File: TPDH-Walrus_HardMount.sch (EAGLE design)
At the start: 37 parts, among them Q2 DMG3404, U1 MS5803-14BA, U2 SN65HVD33RHL, U4 MCP3421A3, U5 TPS79733, U6 MAX6070AAUT18, U7 TXS0102DQM

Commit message: Initial layout for Hard mount (v0.1) variant, cleanup required
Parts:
- removed C11: 10uF, bschulz:C-EU10UFC0805
- removed C7, C8: 0.1uF, bschulz_passives:C-EU0.1UFC0402
- removed H2, H3: (no value), bschulz:MOUNTING_HOLE2_NP
- removed JP1: JUMPER-SMT_3_1-NC_PASTE_SILK, SparkFun-Jumpers:JUMPER-SMT_3_1-NC_PASTE_SILK
- removed R7: (no value), bschulz_passives:R-EU_100R0402
- removed RREF: 10k, bschulz_passives:R-EU_P10KR0603
- removed THERM: 10k, bschulz:THERMISTOR10K
- removed U6: MAX6070AAUT18, bschulz:MAX6070AAUT18
- added D2: (no value), bschulz:TVSSM712
- added U8: NS5A4684S, bschulz:NS5A4684S
- C6: value 0.1uF -> (none)
- U2: value SN65HVD33RHL -> SN65HVD72DSOIC; device bschulz:SN65HVD33RHL -> bschulz:SN65HVD72DSOIC
- U4: value MCP3421A3 -> MCP9808DFNMSOP; device bschulz:MCP3421A3 -> bschulz:MCP9808DFNMSOP
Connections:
- removed net N$11: C7.1, U6.FILT
- removed net SPI-I2C-SWITCH: JP1.2, U1.AD/CS
- removed net VREF: C6.1, THERM.2, U4.VIN+, U6.OUTF, U6.OUTS
- removed net VTHERM-: RREF.2, THERM.1, U4.VIN-
- new net OUTPUT_SEL: U8.IN1, U8.IN2
- new net TEMP_ALERT: U4.ALERT
- net +3V3: now also C6.1, U8.VCC; no longer C11.1, C8.1, JP1.1, U6.VIN
- net A: now also U8.NO2; no longer R7.2, U2.Y
- net B: now also U8.NO1; no longer R7.1, U2.Z
- net GND: now also D2.COM, U1.AD/CS, U4.A0, U4.A1, U4.A2, U4.GND, U8.GND; no longer C11.2, C7.2, C8.2, JP1.3, RREF.1, U4.VSS, U6.GND
- net REF_EN: no longer U6.EN
- net SCL_HV: now also U8.NC2
- net SDA_HV: now also U8.NC1
- net SIG1: now also D2.D1, U8.COM2
- net SIG2: now also D2.D2, U8.COM1
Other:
- note added: "Add temp alert!"
- moved on the sheet: C6

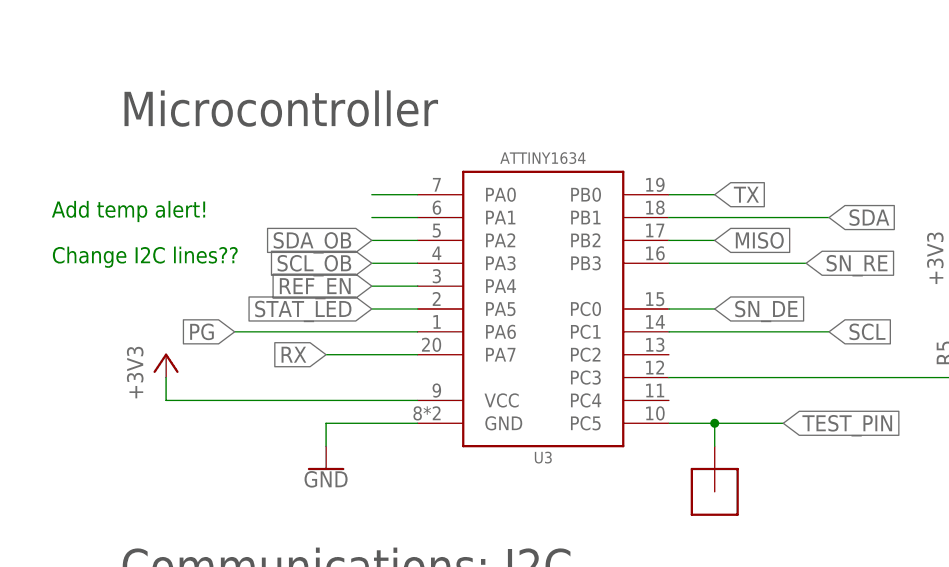
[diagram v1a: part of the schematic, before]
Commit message: Continued layout, final cleanup required
Cleanup and pours required
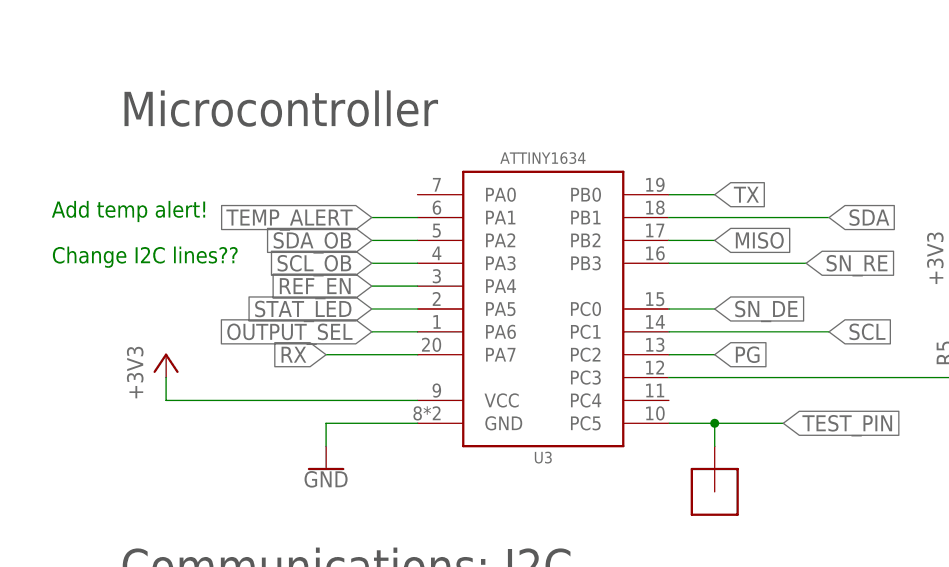
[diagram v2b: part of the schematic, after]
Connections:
- removed net N$1: U3.PA0
- removed net N$3: U3.PA1
- net OUTPUT_SEL: now also U3.PA6
- net PG: now also U3.PC2; no longer U3.PA6
- net TEMP_ALERT: now also U3.PA1
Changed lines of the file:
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@@
 </segment>
 <segment>
-<pinref part="U3" gate="G$1" pin="PA6"/>
-<wire x1="187.96" y1="99.06" x2="167.64" y2="99.06" width="0.1524" layer="91"/>
-<label x="167.64" y="99.06" size="1.778" layer="95" rot="R180" xref="yes"/>
+<pinref part="U3" gate="G$1" pin="PC2"/>
+<wire x1="215.9" y1="96.52" x2="220.98" y2="96.52" width="0.1524" layer="91"/>
+<label x="220.98" y="96.52" size="1.778" layer="95" xref="yes"/>
 </segment>
 </net>
@@
 </segment>
 </net>
-<net name="N$1" class="0">
-<segment>
-<pinref part="U3" gate="G$1" pin="PA0"/>
-<wire x1="187.96" y1="114.3" x2="182.88" y2="114.3" width="0.1524" layer="91"/>
-</segment>
-</net>
-<net name="N$3" class="0">
-<segment>
-<pinref part="U3" gate="G$1" pin="PA1"/>
-<wire x1="187.96" y1="111.76" x2="182.88" y2="111.76" width="0.1524" layer="91"/>
-</segment>
-</net>
 <net name="SDA_OB" class="0">
 <segment>
@@
 <label x="15.24" y="124.46" size="1.778" layer="95"/>
 </segment>
+<segment>
+<pinref part="U3" gate="G$1" pin="PA1"/>
+<wire x1="187.96" y1="111.76" x2="182.88" y2="111.76" width="0.1524" layer="91"/>
+<label x="182.88" y="111.76" size="1.778" layer="95" rot="R180" xref="yes"/>
+</segment>
 </net>
 <net name="OUTPUT_SEL" class="0">
@@
 <label x="68.58" y="137.16" size="1.778" layer="95"/>
 </segment>
-</net>
+<segment>
+<pinref part="U3" gate="G$1" pin="PA6"/>
+<wire x1="187.96" y1="99.06" x2="182.88" y2="99.06" width="0.1524" layer="91"/>
+<label x="182.88" y="99.06" size="1.778" layer="95" rot="R180" xref="yes"/>
+</segment>
+</net>

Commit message: Minor layout updates, sent to fab
Cleaned up layout, sent to fab
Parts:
- U4: value MCP9808DFNMSOP -> MCP9808MSOP; device bschulz:MCP9808DFNMSOP -> bschulz:MCP9808MSOP
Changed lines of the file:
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@@
 <part name="U8" library="bschulz" deviceset="NS5A4684S" device=""/>
 <part name="U2" library="bschulz" deviceset="SN65HVD72" device="SOIC" technology="D"/>
-<part name="U4" library="bschulz" deviceset="MCP9808" device="MSOP" technology="DFN"/>
+<part name="U4" library="bschulz" deviceset="MCP9808" device="MSOP"/>
 <part name="GND4" library="supply1" library_urn="urn:adsk.eagle:library:371" deviceset="GND" device=""/>
 <part name="C6" library="bschulz_passives" deviceset="C-EU" device="C0402" technology="0.1UF"/>

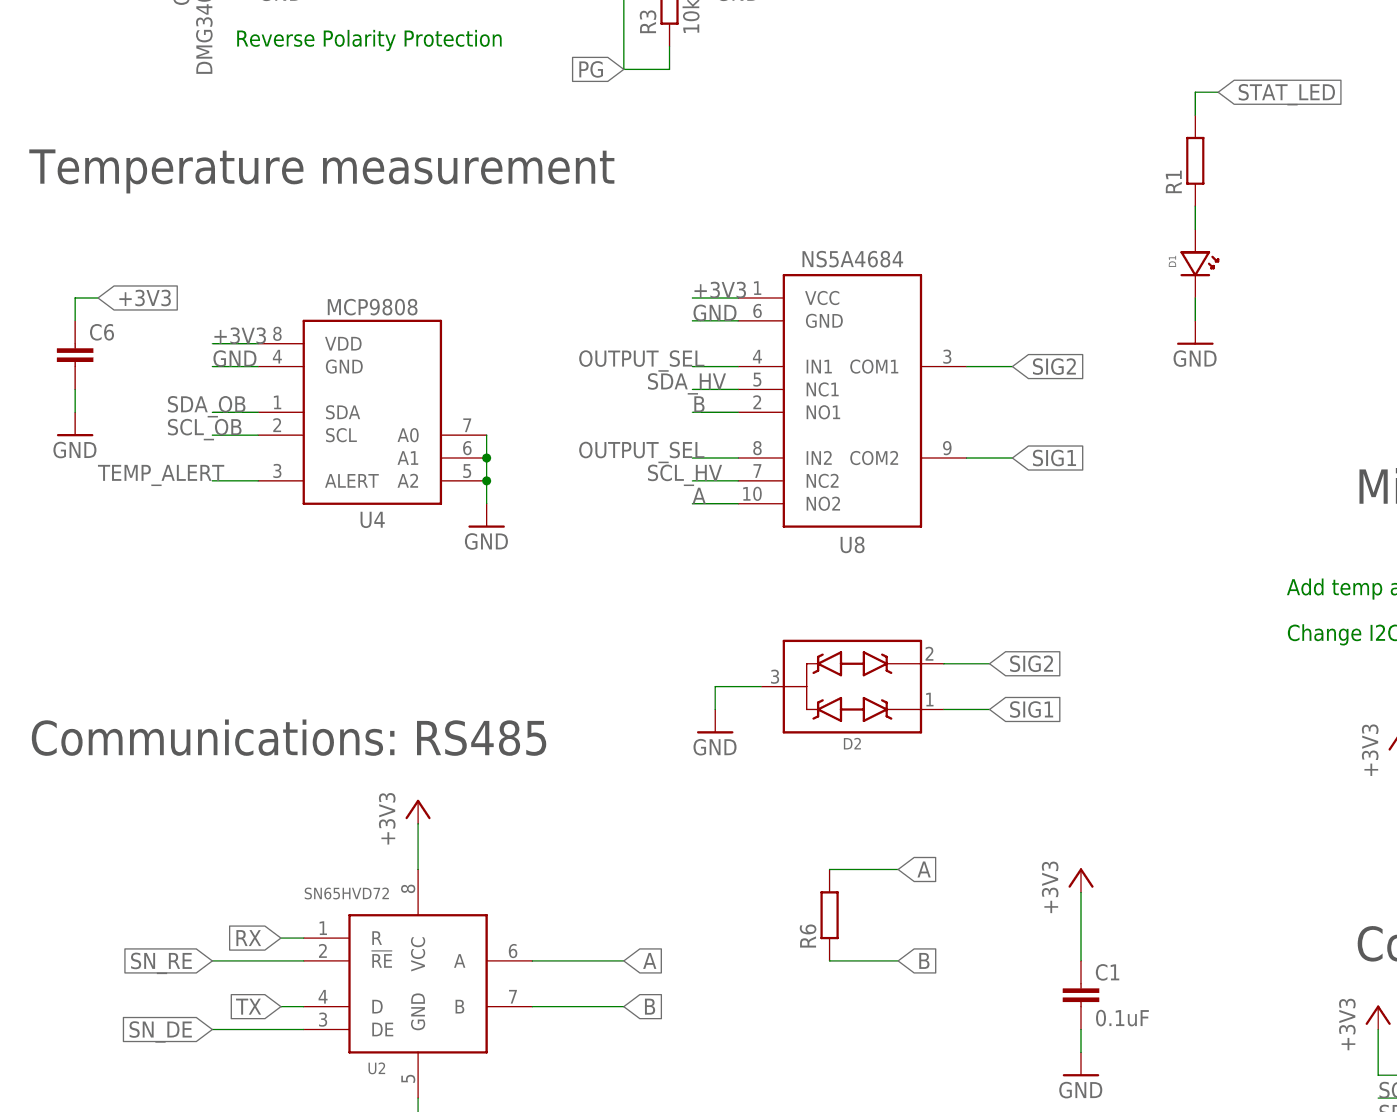
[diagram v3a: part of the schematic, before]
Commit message: Added BOM for hard mount, minor part number cleanup
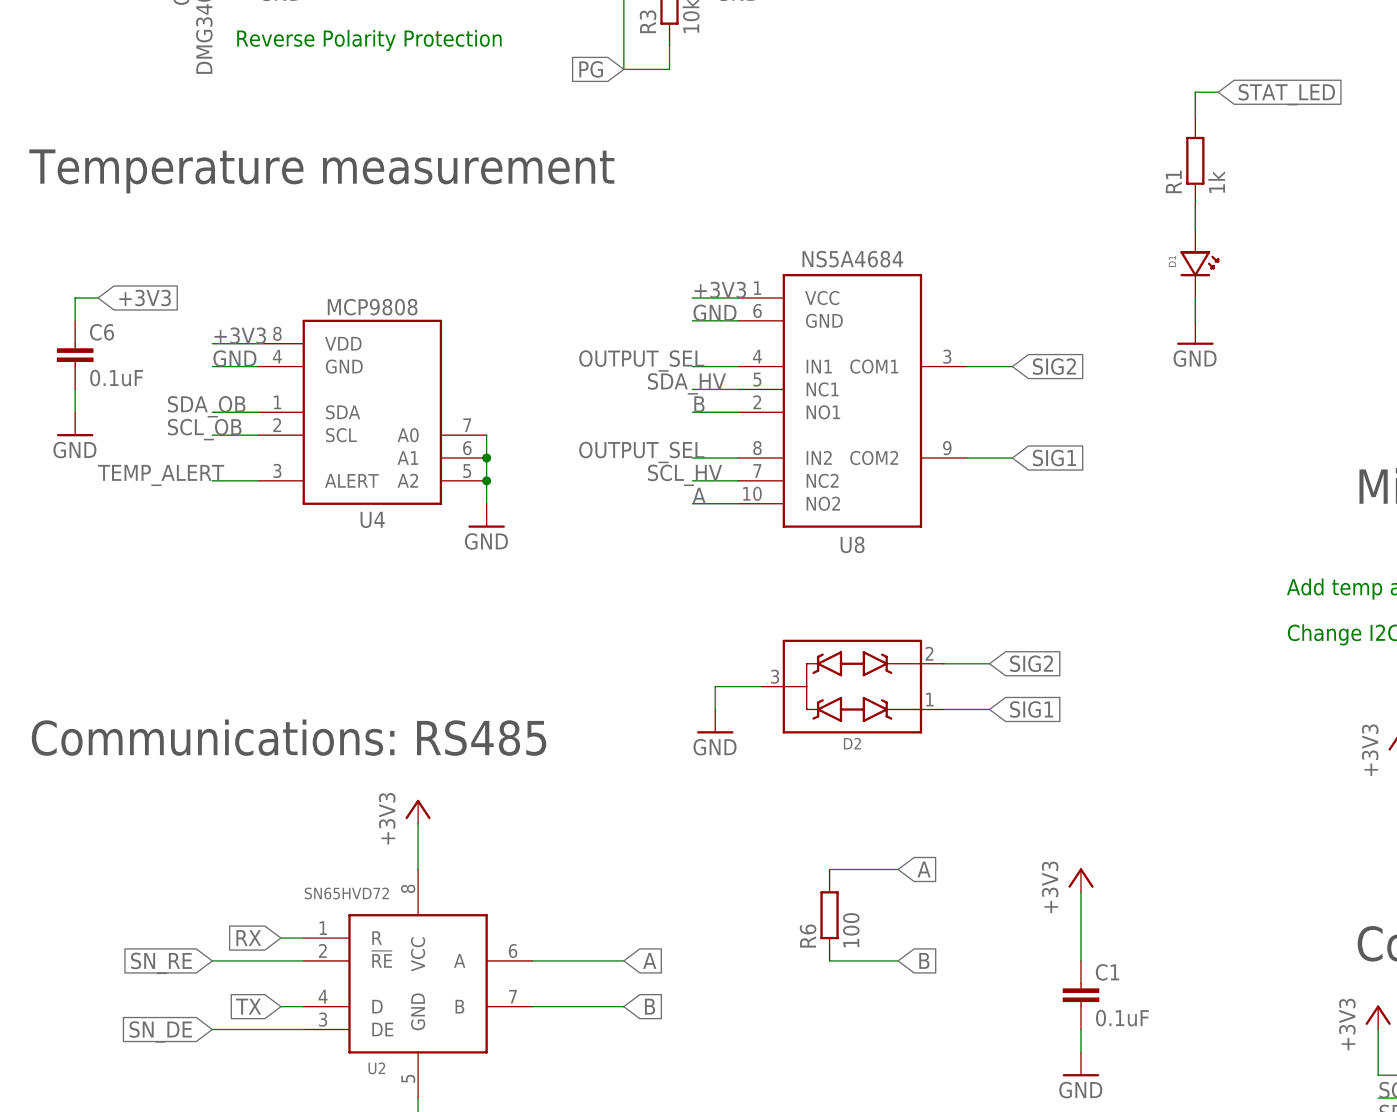
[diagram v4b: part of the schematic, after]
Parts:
- C6: value (none) -> 0.1uF
- R1: value (none) -> 1k
- R6: value (none) -> 100
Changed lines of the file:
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@@
 <?xml version="1.0" encoding="utf-8"?>
 <!DOCTYPE eagle SYSTEM "eagle.dtd">
-<eagle version="9.4.2">
+<eagle version="9.2.1">
 <drawing>
 <settings>
@@
 <part name="R5" library="bschulz_passives" deviceset="R-EU_" device="R0402" technology="10K" value="10k"/>
 <part name="U$12" library="bschulz" deviceset="POGO_PAD" device=""/>
-<part name="R6" library="bschulz_passives" deviceset="R-EU_" device="R0402" technology="100"/>
+<part name="R6" library="bschulz_passives" deviceset="R-EU_" device="R0402" technology="100" value="100"/>
 <part name="U5" library="bschulz" deviceset="TPS797*" device="" technology="33"/>
 <part name="C4" library="bschulz_passives" deviceset="C-EU" device="C0402" technology="0.1UF" value="0.1uF"/>
@@
 <part name="LOGO1" library="SparkFun-Aesthetics" deviceset="OSHW-LOGO" device="M"/>
 <part name="D1" library="bschulz" deviceset="LED" device="0603" technology="BLUE"/>
-<part name="R1" library="bschulz_passives" deviceset="R-EU_" device="R0402"/>
+<part name="R1" library="bschulz_passives" deviceset="R-EU_" device="R0402" value="1k"/>
 <part name="GND20" library="supply1" library_urn="urn:adsk.eagle:library:371" deviceset="GND" device=""/>
 <part name="U$1" library="bschulz" deviceset="SOLDERCUP_CONN_QUAD" device=""/>
@@
 <part name="U4" library="bschulz" deviceset="MCP9808" device="MSOP"/>
 <part name="GND4" library="supply1" library_urn="urn:adsk.eagle:library:371" deviceset="GND" device=""/>
-<part name="C6" library="bschulz_passives" deviceset="C-EU" device="C0402" technology="0.1UF"/>
+<part name="C6" library="bschulz_passives" deviceset="C-EU" device="C0402" technology="0.1UF" value="0.1uF"/>
 <part name="GND5" library="supply1" library_urn="urn:adsk.eagle:library:371" deviceset="GND" device=""/>
 <part name="D2" library="bschulz" deviceset="TVS" device="SM712"/>

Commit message: Update to v0.1 hardware, review required
Initial update complete, requires review and verification of various fixes
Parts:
- added R2: 10k, bschulz_passives:R-EU_10KR0402
- C4: value 0.1uF -> 1uF; device bschulz_passives:C-EU0.1UFC0402 -> bschulz:C-EU1UFC0603
- C5: device bschulz_passives:C-EU1UFC0603 -> bschulz:C-EU1UFC0603
- R1: device bschulz_passives:R-EU_R0402 -> bschulz_passives:R-EU_1KR0603
- U5: value TPS79733 -> LP39883.3VDBV; device bschulz:TPS79733 -> bschulz:LP39883.3VDBV
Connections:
- removed net /RESET: ISP1.RST, R5.1, U3.PC3
- new net !RESET: ISP1.RST, R5.1, U3.PC3, U5.PG
- net +3V3: now also R2.2; no longer U8.VCC
- net PG: no longer R3.1, U5.PG
- net SCL_HV: now also U8.NC1; no longer U8.NC2
- net SCL_OB: now also R2.1
- net SDA_HV: now also U8.NC2; no longer U8.NC1
- net SDA_OB: now also R3.1
- net VIN+: now also U5.EN, U8.VCC
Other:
- moved on the sheet: C5, R3
